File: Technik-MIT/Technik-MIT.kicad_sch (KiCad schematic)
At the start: 16 parts, among them J1 USB_C_Receptacle_USB2.0, U1 RP2040

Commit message: Update PCB schematics (again)
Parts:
- added C11, C12: 10u, symbol Device:C_Small
- added C13, C14: 27p, symbol Device:C_Small
- added R5: 1k, symbol Device:R_Small
- added U2: TVS0500DRV, Package_SON:WSON-6-1EP_2x2mm_P0.65mm_EP1x1.6mm, symbol Power_Protection:TVS0500DRV
- added U3: NCP1117-3.3_SOT223, Package_TO_SOT_SMD:SOT-223-3_TabPin2, symbol Regulator_Linear:NCP1117-3.3_SOT223
- added U4: USBLC6-2SC6, Package_TO_SOT_SMD:SOT-23-6, symbol Power_Protection:USBLC6-2SC6
- added U5: W25Q32JVSS, Package_SO:SOIC-8_5.23x5.23mm_P1.27mm, symbol Memory_Flash:W25Q32JVSS
- added Y1: Crystal, symbol Device:Crystal
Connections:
- net +3V3: now also C12.1, U3.2 (VO), U5.8 (VCC)
- net GND: now also U1.19 (TESTEN), U1.57 (GND), C11.2, C12.2, C13.1, C14.1, U2.1 (GND), U2.2 (GND), U2.3 (GND), U2.7 (GND), U3.1 (GND), U4.2 (GND), U5.4 (GND)
- net USB_D+: now also U4.4 (I/O2); no longer J1.A6 (D+), J1.B6 (D+)
- net USB_D-: now also U4.6 (I/O1); no longer J1.A7 (D-), J1.B7 (D-)
- net VBUS: now also C11.1, U2.4 (IN), U2.5 (IN), U2.6 (IN), U3.3 (VI), U4.5 (VBUS)
- net at U1.20 (XIN): now also C13.2, Y1.2
- net at U1.21 (XOUT): now also R5.2
- net QSPI_SD3: now reaches U1.51 (QSPI_SD3)
- net QSPI_SD3: now also U5.7 (IO3)
- net QSPI_SCLK: now reaches U1.52 (QSPI_SCLK)
- net QSPI_SCLK: now also U5.6 (CLK)
- net QSPI_SD0: now reaches U1.53 (QSPI_SD0)
- net QSPI_SD0: now also U5.5 (DI(IO0))
- net QSPI_SD2: now reaches U1.54 (QSPI_SD2)
- net QSPI_SD2: now also U5.3 (IO2)
- net QSPI_SD1: now reaches U1.55 (QSPI_SD1)
- net QSPI_SD1: now also U5.2 (DO(IO1))
- net QSPI_SS: now reaches U1.56 (QSPI_SS)
- net QSPI_SS: now also U5.1 (~{CS})
- new net: J1.A6 (D+), J1.B6 (D+), U4.3 (I/O2)
- new net: J1.A7 (D-), J1.B7 (D-), U4.1 (I/O1)
- new net: C14.2, R5.1, Y1.1
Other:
- moved on the sheet: C1, C10, C2, C3, C4, C5, C6, C7, C8, C9, J1, R1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

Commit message: Update PCB schematic
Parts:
- added C3: 100n, symbol Device:C_Small
- added D1, D10, D11, D12, D13, D14, D15, D16, D17, D18, D19, D2, D20, D21, D22, D23, D24, D25, D26, D27, D28, D29, D3, D30, D31, D32, D33, D34, D35, D36, D37, D38, D39, D4, D40, D41, D42, D43, D44, D45, D46, D47, D48, D5, D6, D7, D8, D9: 1N4148, Diode_THT:D_DO-35_SOD27_P7.62mm_Horizontal, symbol Diode:1N4148
- added DIP1: BOOTSEL, symbol Switch:SW_DIP_x01
- added R3: 1k, symbol Device:R_Small
- added SW1, SW10, SW11, SW12, SW13, SW14, SW15, SW16, SW17, SW18, SW19, SW2, SW20, SW21, SW22, SW23, SW24, SW25, SW26, SW27, SW28, SW29, SW3, SW30, SW31, SW32, SW33, SW34, SW35, SW36, SW37, SW38, SW39, SW4, SW40, SW41, SW42, SW43, SW44, SW45, SW46, SW47, SW48, SW5, SW6, SW7, SW8, SW9: SW_Push, symbol Switch:SW_Push
- added SW49: RESET, symbol Switch:SW_Push
- Y1: value Crystal -> 12MHz
- renumbered C11 to C1, C1 to C10, C7 to C11, C4 to C12, C5 to C13, C3 to C14, C2 to C15, C12 to C2, C13 to C4, C14 to C5, C10 to C6, C9 to C7, C6 to C9, R3 to R1, R4 to R2, R1 to R4, R2 to R5, R5 to R6, U4 to U1, U5 to U4, U1 to U5
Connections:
- net +3V3: now also C3.1
- net GND: now also C3.2, DIP1.1, SW49.1
- net QSPI_SS: now also R3.2
- net ROW2: now reaches U5.11 (GPIO8)
- net ROW2: now also D11.1 (K), D19.1 (K), D27.1 (K), D3.1 (K), D35.1 (K), D43.1 (K)
- net ROW3: now reaches U5.12 (GPIO9)
- net ROW3: now also D12.1 (K), D20.1 (K), D28.1 (K), D36.1 (K), D4.1 (K), D44.1 (K)
- net ROW4: now reaches U5.13 (GPIO10)
- net ROW4: now also D13.1 (K), D21.1 (K), D29.1 (K), D37.1 (K), D45.1 (K), D5.1 (K)
- net ROW5: now reaches U5.14 (GPIO11)
- net ROW5: now also D14.1 (K), D22.1 (K), D30.1 (K), D38.1 (K), D46.1 (K), D6.1 (K)
- net ROW6: now reaches U5.15 (GPIO12)
- net ROW6: now also D15.1 (K), D23.1 (K), D31.1 (K), D39.1 (K), D47.1 (K), D7.1 (K)
- net ROW7: now reaches U5.16 (GPIO13)
- net ROW7: now also D16.1 (K), D24.1 (K), D32.1 (K), D40.1 (K), D48.1 (K), D8.1 (K)
- net COL0: now reaches U5.2 (GPIO0)
- net COL0: now also SW1.1, SW2.1, SW3.1, SW4.1, SW5.1, SW6.1, SW7.1, SW8.1
- net SWCLK: now reaches U5.24 (SWCLK)
- net SWD: now reaches U5.25 (SWD)
- net at U5.26 (RUN): now also SW49.2
- net COL1: now reaches U5.3 (GPIO1)
- net COL1: now also SW10.1, SW11.1, SW12.1, SW13.1, SW14.1, SW15.1, SW16.1, SW9.1
- net COL2: now reaches U5.4 (GPIO2)
- net COL2: now also SW17.1, SW18.1, SW19.1, SW20.1, SW21.1, SW22.1, SW23.1, SW24.1
- net COL3: now reaches U5.5 (GPIO3)
- net COL3: now also SW25.1, SW26.1, SW27.1, SW28.1, SW29.1, SW30.1, SW31.1, SW32.1
- net COL4: now reaches U5.6 (GPIO4)
- net COL4: now also SW33.1, SW34.1, SW35.1, SW36.1, SW37.1, SW38.1, SW39.1, SW40.1
- net COL5: now reaches U5.7 (GPIO5)
- net COL5: now also SW41.1, SW42.1, SW43.1, SW44.1, SW45.1, SW46.1, SW47.1, SW48.1
- net ROW0: now reaches U5.8 (GPIO6)
- net ROW0: now also D1.1 (K), D17.1 (K), D25.1 (K), D33.1 (K), D41.1 (K), D9.1 (K)
- net ROW1: now reaches U5.9 (GPIO7)
- net ROW1: now also D10.1 (K), D18.1 (K), D2.1 (K), D26.1 (K), D34.1 (K), D42.1 (K)
- new net: D15.2 (A), SW15.2
- new net: D33.2 (A), SW33.2
- new net: D16.2 (A), SW16.2
- new net: D14.2 (A), SW14.2
- new net: D30.2 (A), SW30.2
- new net: D11.2 (A), SW11.2
- new net: D23.2 (A), SW23.2
- new net: D1.2 (A), SW1.2
- new net: D45.2 (A), SW45.2
- new net: D32.2 (A), SW32.2
- new net: D41.2 (A), SW41.2
- new net: D48.2 (A), SW48.2
- new net: D22.2 (A), SW22.2
- new net: D29.2 (A), SW29.2
- new net: D21.2 (A), SW21.2
- new net: D17.2 (A), SW17.2
- new net: D12.2 (A), SW12.2
- new net: D8.2 (A), SW8.2
- new net: D25.2 (A), SW25.2
- new net: D18.2 (A), SW18.2
- new net: DIP1.2, R3.1
- new net: D36.2 (A), SW36.2
- new net: D24.2 (A), SW24.2
- new net: D9.2 (A), SW9.2
- new net: D2.2 (A), SW2.2
- new net: D38.2 (A), SW38.2
- new net: D35.2 (A), SW35.2
- new net: D43.2 (A), SW43.2
- new net: D19.2 (A), SW19.2
- new net: D31.2 (A), SW31.2
- new net: D10.2 (A), SW10.2
- new net: D13.2 (A), SW13.2
- new net: D39.2 (A), SW39.2
- new net: D27.2 (A), SW27.2
- new net: D26.2 (A), SW26.2
- new net: D47.2 (A), SW47.2
- new net: D28.2 (A), SW28.2
- new net: D40.2 (A), SW40.2
- new net: D37.2 (A), SW37.2
- new net: D4.2 (A), SW4.2
- new net: D46.2 (A), SW46.2
- new net: D6.2 (A), SW6.2
- new net: D3.2 (A), SW3.2
- new net: D42.2 (A), SW42.2
- new net: D34.2 (A), SW34.2
- new net: D7.2 (A), SW7.2
- new net: D20.2 (A), SW20.2
- new net: D44.2 (A), SW44.2
- new net: D5.2 (A), SW5.2
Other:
- moved on the sheet: C1, C10, C11, C12, C13, C14, C15, C2, C4, C5, C6, C7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

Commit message: Update PCB
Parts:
- added SW50: SW_Push, kbd:ChocV1_Hotswap, symbol Switch:SW_Push
- C1, C10, C11, C12, C13, C14, C15, C2, C3, C4, C5, C6, C7, C8, C9: footprint (none) -> Capacitor_SMD:C_0402_1005Metric
- D1, D10, D11, D12, D13, D14, D15, D16, D17, D18, D19, D2, D20, D21, D22, D23, D24, D25, D26, D27, D28, D29, D3, D30, D31, D32, D33, D34, D35, D36, D37, D38, D39, D4, D40, D41, D42, D43, D44, D45, D46, D47, D48, D5, D6, D7, D8, D9: footprint Diode_THT:D_DO-35_SOD27_P7.62mm_Horizontal -> Diode_SMD:D_SOD-123
- DIP1: footprint (none) -> Button_Switch_SMD:SW_DIP_SPSTx01_Slide_6.7x4.1mm_W8.61mm_P2.54mm_LowProfile
- J1: footprint (none) -> Connector_USB:USB_C_Receptacle_Molex_105450-0101
- R1, R2, R3, R4, R5, R6: footprint (none) -> Resistor_SMD:R_0402_1005Metric
- SW1, SW10, SW11, SW12, SW13, SW14, SW15, SW16, SW17, SW18, SW19, SW2, SW20, SW21, SW22, SW23, SW24, SW25, SW26, SW27, SW28, SW29, SW3, SW30, SW31, SW32, SW33, SW34, SW35, SW36, SW37, SW38, SW39, SW4, SW40, SW41, SW42, SW43, SW44, SW45, SW46, SW47, SW48, SW5, SW6, SW7, SW8, SW9: footprint (none) -> kbd:ChocV1_Hotswap
- SW49: footprint (none) -> Button_Switch_SMD:SW_SPST_B3U-1000P
- Y1: footprint (none) -> Crystal:Crystal_SMD_7050-4Pin_7.0x5.0mm
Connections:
- net COL2: now also SW50.2
- net at D24.2 (A), SW24.2: now also SW50.1
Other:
- moved on the sheet: C1, C10, C11, C12, C13, C14, C15, C2, C3, C4, C5, C6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

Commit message: Working on PCB
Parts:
- removed U3: NCP1117-3.3_SOT223, Package_TO_SOT_SMD:SOT-223-3_TabPin2, symbol Regulator_Linear:NCP1117-3.3_SOT223
- removed Y1: 12MHz, Crystal:Crystal_SMD_7050-4Pin_7.0x5.0mm, symbol Device:Crystal
- added U3: AP2127N-3.3, Package_TO_SOT_SMD:SOT-23, symbol Regulator_Linear:AP2127N-3.3
- added Y1: Crystal_GND24, symbol Device:Crystal_GND24
- J1: footprint Connector_USB:USB_C_Receptacle_Molex_105450-0101 -> molex-216990_gct-usb45xx_hro-type-c-31-m-13x:Molex-216990_GCT-USB45xx_HRO-TYPE-C-31-M-13x
- SW1, SW10, SW11, SW12, SW13, SW14, SW15, SW16, SW17, SW18, SW19, SW2, SW20, SW21, SW22, SW23, SW24, SW25, SW26, SW27, SW28, SW29, SW3, SW30, SW31, SW32, SW33, SW34, SW35, SW36, SW37, SW38, SW39, SW4, SW40, SW41, SW42, SW43, SW44, SW45, SW46, SW47, SW48, SW5, SW50, SW6, SW7, SW8, SW9: footprint kbd:ChocV1_Hotswap -> Technik-MIT:ChocV1_Hotswap
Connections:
- net +3V3: now also U3.2 (VO)
- net GND: now also U3.1 (GND), Y1.2, Y1.4
- net VBUS: now also U3.3 (VI)
- net at C4.2, U5.20 (XIN): now also Y1.1
- net at C5.2, R6.1: now also Y1.3
- no-connect marks 2 -> 18

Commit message: Working on PCB
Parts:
- removed DIP1: BOOTSEL, Button_Switch_SMD:SW_DIP_SPSTx01_Slide_6.7x4.1mm_W8.61mm_P2.54mm_LowProfile, symbol Switch:SW_DIP_x01
- added DIP1: BOOTSEL, Button_Switch_SMD:SW_SPDT_PCM12, symbol Switch:SW_SPDT
- Y1: footprint (none) -> Crystal:Crystal_SMD_3225-4Pin_3.2x2.5mm
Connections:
- net GND: now also DIP1.2 (B), DIP1.3 (C)
- net at R3.1: now also DIP1.1 (A)
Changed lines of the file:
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@@
   (junction (at 39.37 119.38) (diameter 0) (color 0 0 0 0)
   )
+  (junction (at 101.6 54.61) (diameter 0) (color 0 0 0 0)
+  )
   (junction (at 260.35 21.59) (diameter 0) (color 0 0 0 0)
   )
@@
     (stroke (width 0) (type default))
   )
+  (wire (pts (xy 101.6 49.53) (xy 101.6 54.61))
+    (stroke (width 0) (type default))
+  )
   (wire (pts (xy 19.05 66.04) (xy 26.67 66.04))
     (stroke (width 0) (type default))
@@
     (stroke (width 0) (type default))
   )
-  (wire (pts (xy 100.33 46.99) (xy 100.33 52.07))
+  (wire (pts (xy 118.11 54.61) (xy 101.6 54.61))
     (stroke (width 0) (type default))
   )
@@
     (stroke (width 0) (type default))
   )
-  (wire (pts (xy 118.11 46.99) (xy 120.65 46.99))
+  (wire (pts (xy 115.57 46.99) (xy 120.65 46.99))
     (stroke (width 0) (type default))
   )
@@
     (stroke (width 0) (type default))
   )
+  (wire (pts (xy 118.11 52.07) (xy 115.57 52.07))
+    (stroke (width 0) (type default))
+  )
   (wire (pts (xy 217.17 21.59) (xy 217.17 33.02))
     (stroke (width 0) (type default))
@@
     (stroke (width 0) (type default))
   )
+  (wire (pts (xy 118.11 52.07) (xy 118.11 54.61))
+    (stroke (width 0) (type default))
+  )
   (wire (pts (xy 44.45 36.83) (xy 44.45 34.29))
     (stroke (width 0) (type default))
@@
     (stroke (width 0) (type default))
   )
-  (wire (pts (xy 102.87 46.99) (xy 100.33 46.99))
-    (stroke (width 0) (type default))
-  )
   (wire (pts (xy 39.37 132.08) (xy 60.96 132.08))
     (stroke (width 0) (type default))
@@
     (stroke (width 0) (type default))
   )
+  (wire (pts (xy 101.6 49.53) (xy 105.41 49.53))
+    (stroke (width 0) (type default))
+  )
   (wire (pts (xy 222.25 138.43) (xy 222.25 137.16))
     (stroke (width 0) (type default))
@@
     (stroke (width 0) (type default))
   )
+  (wire (pts (xy 101.6 54.61) (xy 101.6 57.15))
+    (stroke (width 0) (type default))
+  )
   (wire (pts (xy 217.17 43.18) (xy 217.17 45.72))
     (stroke (width 0) (type default))
@@
     )
   )
+  (symbol (lib_id "Switch:SW_SPDT") (at 110.49 49.53 0) (unit 1)
+    (in_bom yes) (on_board yes) (dnp no) (fields_autoplaced)
+    (property "Reference" "DIP1" (at 110.49 43.18 0)
+      (effects (font (size 1.27 1.27)))
+    )
+    (property "Value" "BOOTSEL" (at 110.49 45.72 0)
+      (effects (font (size 1.27 1.27)))
+    )
+    (property "Footprint" "Button_Switch_SMD:SW_SPDT_PCM12" (at 110.49 49.53 0)
+      (effects (font (size 1.27 1.27)) hide)
+    )
+    (property "Datasheet" "~" (at 110.49 49.53 0)
+      (effects (font (size 1.27 1.27)) hide)
+    )
+    (pin "1")
+    (pin "2")
+    (pin "3")
+    (instances
+      (project "Technik-MIT"
+        (path "/cb576f1a-a142-4cba-b8e8-c44522cf16c1"
+          (reference "DIP1") (unit 1)
+        )
+      )
+    )
+  )
   (symbol (lib_id "Switch:SW_Push") (at 77.47 162.56 0) (unit 1)
     (in_bom yes) (on_board yes) (dnp no) (fields_autoplaced)
@@
     )
   )
-  (symbol (lib_id "Switch:SW_DIP_x01") (at 110.49 46.99 0) (unit 1)
-    (in_bom yes) (on_board yes) (dnp no) (fields_autoplaced)
-    (property "Reference" "DIP1" (at 110.49 40.64 0)
-      (effects (font (size 1.27 1.27)))
-    )
-    (property "Value" "BOOTSEL" (at 110.49 43.18 0)
-      (effects (font (size 1.27 1.27)))
-    )
-    (property "Footprint" "Button_Switch_SMD:SW_DIP_SPSTx01_Slide_6.7x4.1mm_W8.61mm_P2.54mm_LowProfile" (at 110.49 46.99 0)
-      (effects (font (size 1.27 1.27)) hide)
-    )
-    (property "Datasheet" "~" (at 110.49 46.99 0)
-      (effects (font (size 1.27 1.27)) hide)
-    )
-    (pin "1")
-    (pin "2")
-    (instances
-      (project "Technik-MIT"
-        (path "/cb576f1a-a142-4cba-b8e8-c44522cf16c1"
-          (reference "DIP1") (unit 1)
-        )
-      )
-    )
-  )
   (symbol (lib_id "Switch:SW_Push") (at 77.47 137.16 0) (unit 1)
     (in_bom yes) (on_board yes) (dnp no) (fields_autoplaced)
@@
     )
   )
-  (symbol (lib_id "power:GND") (at 100.33 52.07 0) (unit 1)
+  (symbol (lib_id "power:GND") (at 101.6 57.15 0) (unit 1)
     (in_bom yes) (on_board yes) (dnp no) (fields_autoplaced)
-    (property "Reference" "#PWR08" (at 100.33 58.42 0)
+    (property "Reference" "#PWR08" (at 101.6 63.5 0)
       (effects (font (size 1.27 1.27)) hide)
     )
-    (property "Value" "GND" (at 100.33 57.15 0)
+    (property "Value" "GND" (at 101.6 62.23 0)
       (effects (font (size 1.27 1.27)))
     )
-    (property "Footprint" "" (at 100.33 52.07 0)
+    (property "Footprint" "" (at 101.6 57.15 0)
       (effects (font (size 1.27 1.27)) hide)
     )
-    (property "Datasheet" "" (at 100.33 52.07 0)
+    (property "Datasheet" "" (at 101.6 57.15 0)
       (effects (font (size 1.27 1.27)) hide)
     )
@@
       (effects (font (size 1.27 1.27)))
     )
-    (property "Footprint" "" (at 181.61 104.14 0)
+    (property "Footprint" "Crystal:Crystal_SMD_3225-4Pin_3.2x2.5mm" (at 181.61 104.14 0)
       (effects (font (size 1.27 1.27)) hide)
     )

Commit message: Update PCB
Change spacing from MX to Choc
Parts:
- removed D28: 1N4148, Diode_SMD:D_SOD-123, symbol Diode:1N4148
- removed SW24, SW28: SW_Push, Technik-MIT:ChocV1_Hotswap, symbol Switch:SW_Push
- C1, C2: value 10u -> 1u
- renumbered D29 to D28, D30 to D29, D31 to D30, D32 to D31, D33 to D32, D34 to D33, D35 to D34, D36 to D35, D37 to D36, D38 to D37, D39 to D38, D40 to D39, D41 to D40, D42 to D41, D43 to D42, D44 to D43, D45 to D44, D46 to D45, D47 to D46, D48 to D47, SW50 to SW24, SW29 to SW28, SW30 to SW29, SW31 to SW30, SW32 to SW31, SW33 to SW32, SW34 to SW33, SW35 to SW34, SW36 to SW35, SW37 to SW36, SW38 to SW37, SW39 to SW38, SW40 to SW39, SW41 to SW40, SW42 to SW41, SW43 to SW42, SW44 to SW43, SW45 to SW44, SW46 to SW45, SW47 to SW46, SW48 to SW47, SW49 to SW48
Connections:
- net COL0: now also U5.36 (GPIO24); no longer U5.2 (GPIO0)
- net COL1: now also U5.37 (GPIO25); no longer U5.3 (GPIO1)
- net COL2: now also SW24.1, U5.38 (GPIO26_ADC0); no longer SW24.2, U5.4 (GPIO2)
- net COL3: now also U5.39 (GPIO27_ADC1); no longer U5.5 (GPIO3)
- net COL4: now also U5.40 (GPIO28_ADC2); no longer U5.6 (GPIO4)
- net COL5: now also U5.41 (GPIO29_ADC3); no longer U5.7 (GPIO5)
- net ROW0: now also U5.3 (GPIO1); no longer U5.8 (GPIO6)
- net ROW1: now also U5.5 (GPIO3); no longer U5.9 (GPIO7)
- net ROW2: now also U5.35 (GPIO23); no longer U5.11 (GPIO8)
- net ROW3: now also U5.30 (GPIO19); no longer U5.12 (GPIO9)
- net ROW4: now also U5.4 (GPIO2); no longer U5.13 (GPIO10)
- net ROW5: now also U5.6 (GPIO4); no longer U5.14 (GPIO11)
- net ROW6: now also U5.31 (GPIO20); no longer U5.15 (GPIO12)
- net ROW7: now also U5.29 (GPIO18); no longer U5.16 (GPIO13)
- net at D24.2 (A): now also SW24.2; no longer SW24.1
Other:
- note added: "Close to VREG_IN"
- note added: "Close to VREG_VOUT"
- note added: "Each close to DVDD"
- note added: "Each close to IOVDD"
- moved on the sheet: D16, D24, D31, D39, D47, D8, SW24

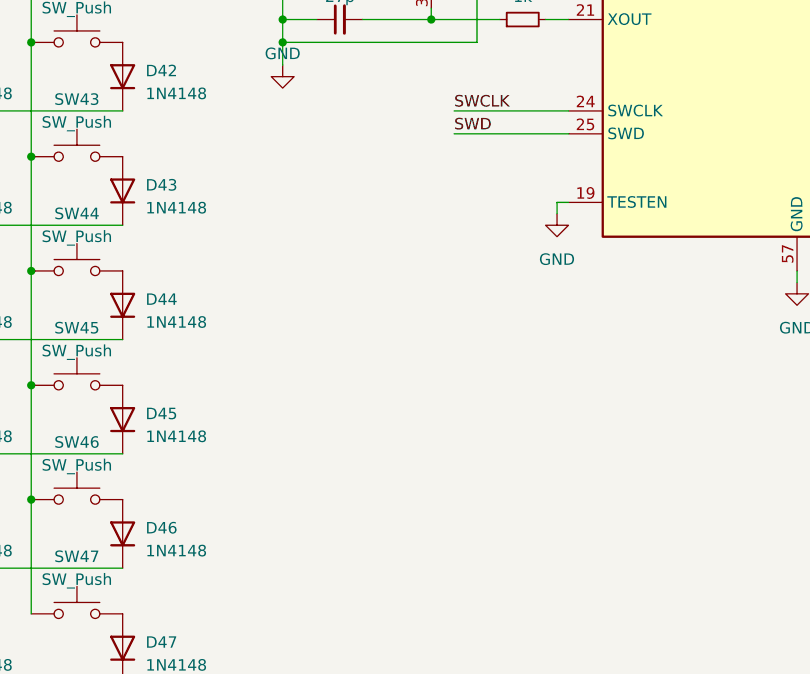
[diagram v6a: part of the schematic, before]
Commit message: Update PCB to match preexisting mounting holes
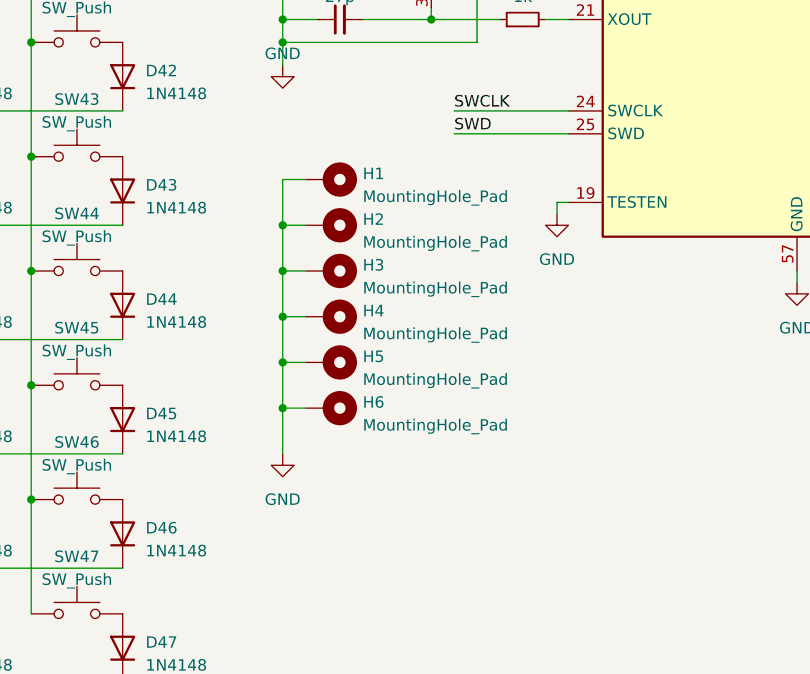
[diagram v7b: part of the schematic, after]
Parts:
- added H1, H2, H3, H4, H5, H6: MountingHole_Pad, Technik-MIT:Standoff_Hole, symbol Mechanical:MountingHole_Pad
- J1: footprint molex-216990_gct-usb45xx_hro-type-c-31-m-13x:Molex-216990_GCT-USB45xx_HRO-TYPE-C-31-M-13x -> Technik-MIT:Molex-216990_GCT-USB45xx_HRO-TYPE-C-31-M-13x
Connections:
- net GND: now also H1.1, H2.1, H3.1, H4.1, H5.1, H6.1

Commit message: Add tooling holes, JLC order number silkscreen.
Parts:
- added H7, H8, H9: MountingHole, Technik-MIT:Tooling Hole, symbol Mechanical:MountingHole
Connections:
- no-connect marks 18 -> 20
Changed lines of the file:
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@@
   (no_connect (at 247.65 91.44))
   (no_connect (at 247.65 106.68))
+  (no_connect (at 184.15 121.92))
   (no_connect (at 41.91 57.15))
   (no_connect (at 247.65 73.66))
@@
   (no_connect (at 41.91 54.61))
   (no_connect (at 247.65 88.9))
+  (no_connect (at 184.15 119.38))
   (no_connect (at 247.65 78.74))
   (no_connect (at 247.65 93.98))
@@
         (path "/cb576f1a-a142-4cba-b8e8-c44522cf16c1"
           (reference "#PWR020") (unit 1)
+        )
+      )
+    )
+  )
+  (symbol (lib_id "Mechanical:MountingHole") (at 236.22 147.32 0) (unit 1)
+    (in_bom yes) (on_board yes) (dnp no) (fields_autoplaced)
+    (property "Reference" "H7" (at 238.76 146.685 0)
+      (effects (font (size 1.27 1.27)) (justify left))
+    )
+    (property "Value" "MountingHole" (at 238.76 149.225 0)
+      (effects (font (size 1.27 1.27)) (justify left))
+    )
+    (property "Footprint" "Technik-MIT:Tooling Hole" (at 236.22 147.32 0)
+      (effects (font (size 1.27 1.27)) hide)
+    )
+    (property "Datasheet" "~" (at 236.22 147.32 0)
+      (effects (font (size 1.27 1.27)) hide)
+    )
+    (instances
+      (project "Technik-MIT"
+        (path "/cb576f1a-a142-4cba-b8e8-c44522cf16c1"
+          (reference "H7") (unit 1)
         )
       )
@@
     )
   )
+  (symbol (lib_id "Mechanical:MountingHole") (at 236.22 157.48 0) (unit 1)
+    (in_bom yes) (on_board yes) (dnp no) (fields_autoplaced)
+    (property "Reference" "H9" (at 238.76 156.845 0)
+      (effects (font (size 1.27 1.27)) (justify left))
+    )
+    (property "Value" "MountingHole" (at 238.76 159.385 0)
+      (effects (font (size 1.27 1.27)) (justify left))
+    )
+    (property "Footprint" "Technik-MIT:Tooling Hole" (at 236.22 157.48 0)
+      (effects (font (size 1.27 1.27)) hide)
+    )
+    (property "Datasheet" "~" (at 236.22 157.48 0)
+      (effects (font (size 1.27 1.27)) hide)
+    )
+    (instances
+      (project "Technik-MIT"
+        (path "/cb576f1a-a142-4cba-b8e8-c44522cf16c1"
+          (reference "H9") (unit 1)
+        )
+      )
+    )
+  )
   (symbol (lib_id "Switch:SW_Push") (at 99.06 149.86 0) (unit 1)
     (in_bom yes) (on_board yes) (dnp no) (fields_autoplaced)
@@
         )
       )
+    )
+  )
+  (symbol (lib_id "Mechanical:MountingHole") (at 236.22 152.4 0) (unit 1)
+    (in_bom yes) (on_board yes) (dnp no) (fields_autoplaced)
+    (property "Reference" "H8" (at 238.76 151.765 0)
+      (effects (font (size 1.27 1.27)) (justify left))
+    )
+    (property "Value" "MountingHole" (at 238.76 154.305 0)
+      (effects (font (size 1.27 1.27)) (justify left))
+    )
+    (property "Footprint" "Technik-MIT:Tooling Hole" (at 236.22 152.4 0)
+      (effects (font (size 1.27 1.27)) hide)
+    )
+    (property "Datasheet" "~" (at 236.22 152.4 0)
+      (effects (font (size 1.27 1.27)) hide)
+    )
+    (instances
+      (project "Technik-MIT"
+        (path "/cb576f1a-a142-4cba-b8e8-c44522cf16c1"
+          (reference "H8") (unit 1)
+        )
+      )
